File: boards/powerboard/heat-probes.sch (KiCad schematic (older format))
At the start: 16 parts, among them J801 Heat probe power, Q801 BUK7Y4R8-60E, Q802 BUK7Y4R8-60E, Q803 BUK7Y4R8-60E, U801 ACS711, U802 ACS711, U803 ACS711

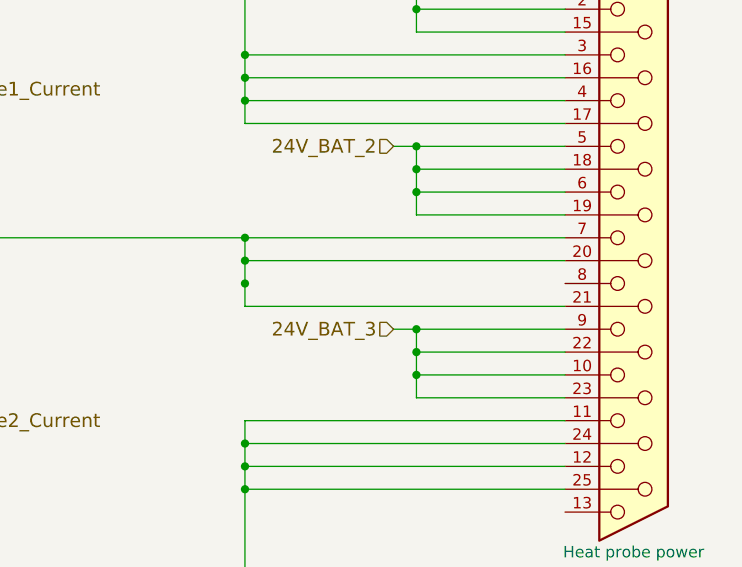
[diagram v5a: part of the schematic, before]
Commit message: [powerboard] layout: parts placed; RS-422 termination added; various minor improvements
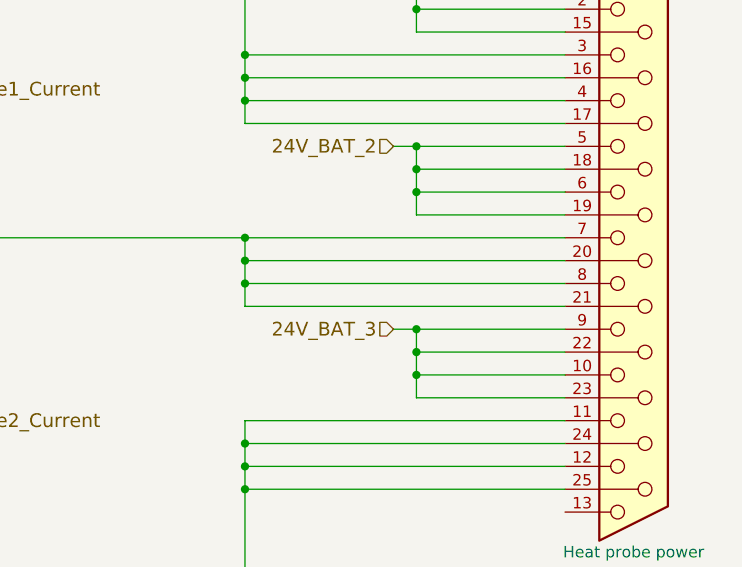
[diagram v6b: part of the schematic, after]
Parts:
- J801: footprint Mounting_Holes:MountingHole_3.2mm_M3_Pad_Via -> Connectors:DB25FD
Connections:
- net at J801.20 (P20), J801.21 (P21), J801.7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: now also J801.8
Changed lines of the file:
@@
 $EndDescr
 $Comp
-L GND #PWR058
+L GND #PWR060
 U 1 1 58F51ACB
 P 6250 5800
-F 0 "#PWR058" H 6250 5550 50  0001 C CNN
+F 0 "#PWR060" H 6250 5550 50  0001 C CNN
 F 1 "GND" H 6250 5650 50  0000 C CNN
 F 2 "" H 6250 5800 50  0000 C CNN
@@
 $EndComp
 $Comp
-L GND #PWR059
+L GND #PWR061
 U 1 1 58F51AEC
 P 5050 5900
-F 0 "#PWR059" H 5050 5650 50  0001 C CNN
+F 0 "#PWR061" H 5050 5650 50  0001 C CNN
 F 1 "GND" H 5050 5750 50  0000 C CNN
 F 2 "" H 5050 5900 50  0000 C CNN
@@
 $EndComp
 $Comp
-L GND #PWR060
+L GND #PWR062
 U 1 1 58F51AF2
 P 5050 3050
-F 0 "#PWR060" H 5050 2800 50  0001 C CNN
+F 0 "#PWR062" H 5050 2800 50  0001 C CNN
 F 1 "GND" H 5050 2900 50  0000 C CNN
 F 2 "" H 5050 3050 50  0000 C CNN
@@
 $EndComp
 $Comp
-L GND #PWR061
+L GND #PWR063
 U 1 1 58F51AF8
 P 5050 4500
-F 0 "#PWR061" H 5050 4250 50  0001 C CNN
+F 0 "#PWR063" H 5050 4250 50  0001 C CNN
 F 1 "GND" H 5050 4350 50  0000 C CNN
 F 2 "" H 5050 4500 50  0000 C CNN
@@
 $EndComp
 $Comp
-L GND #PWR062
+L GND #PWR064
 U 1 1 58F51AFE
 P 6250 4400
-F 0 "#PWR062" H 6250 4150 50  0001 C CNN
+F 0 "#PWR064" H 6250 4150 50  0001 C CNN
 F 1 "GND" H 6250 4250 50  0000 C CNN
 F 2 "" H 6250 4400 50  0000 C CNN
@@
 $EndComp
 $Comp
-L GND #PWR063
+L GND #PWR065
 U 1 1 58F51B04
 P 6250 2950
-F 0 "#PWR063" H 6250 2700 50  0001 C CNN
+F 0 "#PWR065" H 6250 2700 50  0001 C CNN
 F 1 "GND" H 6250 2800 50  0000 C CNN
 F 2 "" H 6250 2950 50  0000 C CNN
@@
 $EndComp
 $Comp
-L +3V3 #PWR064
+L +3V3 #PWR066
 U 1 1 58F51B0A
 P 6250 5500
-F 0 "#PWR064" H 6250 5350 50  0001 C CNN
+F 0 "#PWR066" H 6250 5350 50  0001 C CNN
 F 1 "+3V3" H 6250 5640 50  0000 C CNN
 F 2 "" H 6250 5500 50  0000 C CNN
@@
 $EndComp
 $Comp
-L +3V3 #PWR065
+L +3V3 #PWR067
 U 1 1 58F51B10
 P 6250 4100
-F 0 "#PWR065" H 6250 3950 50  0001 C CNN
+F 0 "#PWR067" H 6250 3950 50  0001 C CNN
 F 1 "+3V3" H 6250 4240 50  0000 C CNN
 F 2 "" H 6250 4100 50  0000 C CNN
@@
 $EndComp
 $Comp
-L +3V3 #PWR066
+L +3V3 #PWR068
 U 1 1 58F51B16
 P 6250 2650
-F 0 "#PWR066" H 6250 2500 50  0001 C CNN
+F 0 "#PWR068" H 6250 2500 50  0001 C CNN
 F 1 "+3V3" H 6250 2790 50  0000 C CNN
 F 2 "" H 6250 2650 50  0000 C CNN
@@
 $EndComp
 $Comp
-L +3V3 #PWR067
+L +3V3 #PWR069
 U 1 1 58F51B37
 P 4750 6600
-F 0 "#PWR067" H 4750 6450 50  0001 C CNN
+F 0 "#PWR069" H 4750 6450 50  0001 C CNN
 F 1 "+3V3" H 4750 6740 50  0000 C CNN
 F 2 "" H 4750 6600 50  0000 C CNN
@@
 $EndComp
 $Comp
-L GND #PWR068
+L GND #PWR070
 U 1 1 58F51B3D
 P 4750 7100
-F 0 "#PWR068" H 4750 6850 50  0001 C CNN
+F 0 "#PWR070" H 4750 6850 50  0001 C CNN
 F 1 "GND" H 4750 6950 50  0000 C CNN
 F 2 "" H 4750 7100 50  0000 C CNN
@@
 F 0 "J801" H 10200 4750 50  0000 C CNN
 F 1 "Heat probe power" H 10200 2025 50  0000 C CNN
-F 2 "Mounting_Holes:MountingHole_3.2mm_M3_Pad_Via" H 10200 3400 50  0001 C CNN
+F 2 "Connectors:DB25FD" H 10200 3400 50  0001 C CNN
 F 3 "" H 10200 3400 50  0001 C CNN
 	1    10200 3400
@@
 Connection ~ 8500 3400
 Connection ~ 3800 3200
+Wire Wire Line
+	9900 3600 8500 3600
 $EndSCHEMATC

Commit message: [powerboard] first layout (wip)
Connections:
- net Probe1: now also J801.16 (P16), J801.17 (P17), J801.3, J801.4, Q801.5 (D); no longer Q801.1 (S), Q801.2 (S), Q801.3 (S), R804.1, U801.1 (IP+), U801.2 (IP+)
- net Probe2: now also J801.20 (P20), J801.21 (P21), J801.7, J801.8, Q802.5 (D); no longer Q802.1 (S), Q802.2 (S), Q802.3 (S), R805.1, U802.1 (IP+), U802.2 (IP+)
- net Probe3: now also J801.11, J801.12, J801.24 (P24), J801.25 (P25), Q803.5 (D); no longer Q803.1 (S), Q803.2 (S), Q803.3 (S), R806.1, U803.1 (IP+), U803.2 (IP+)
- new net Probe1_sense: Q801.1 (S), Q801.2 (S), Q801.3 (S), R804.1, U801.1 (IP+), U801.2 (IP+)
- new net Probe2_sense: Q802.1 (S), Q802.2 (S), Q802.3 (S), R805.1, U802.1 (IP+), U802.2 (IP+)
- new net Probe3_sense: Q803.1 (S), Q803.2 (S), Q803.3 (S), R806.1, U803.1 (IP+), U803.2 (IP+)
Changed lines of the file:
@@
 $EndDescr
 $Comp
-L GND #PWR711
+L GND #PWR060
 U 1 1 58F51ACB
 P 6250 5800
-F 0 "#PWR711" H 6250 5550 50  0001 C CNN
+F 0 "#PWR060" H 6250 5550 50  0001 C CNN
 F 1 "GND" H 6250 5650 50  0000 C CNN
 F 2 "" H 6250 5800 50  0000 C CNN
@@
 	0    -1   -1   0
 $EndComp
-Text Label 4450 2750 0    60   ~ 0
-Probe1
-Text Label 4200 4200 0    60   ~ 0
-Probe2
-Text Label 4550 5600 0    60   ~ 0
-Probe3
+Text Label 3900 2750 0    60   ~ 0
+Probe1_sense
+Text Label 3900 4200 0    60   ~ 0
+Probe2_sense
+Text Label 3900 5600 0    60   ~ 0
+Probe3_sense
 Text Label 2800 3900 2    60   ~ 0
 Probe2_EN
@@
 $EndComp
 $Comp
-L GND #PWR705
+L GND #PWR061
 U 1 1 58F51AEC
 P 5050 5900
-F 0 "#PWR705" H 5050 5650 50  0001 C CNN
+F 0 "#PWR061" H 5050 5650 50  0001 C CNN
 F 1 "GND" H 5050 5750 50  0000 C CNN
 F 2 "" H 5050 5900 50  0000 C CNN
@@
 $EndComp
 $Comp
-L GND #PWR703
+L GND #PWR062
 U 1 1 58F51AF2
 P 5050 3050
-F 0 "#PWR703" H 5050 2800 50  0001 C CNN
+F 0 "#PWR062" H 5050 2800 50  0001 C CNN
 F 1 "GND" H 5050 2900 50  0000 C CNN
 F 2 "" H 5050 3050 50  0000 C CNN
@@
 $EndComp
 $Comp
-L GND #PWR704
+L GND #PWR063
 U 1 1 58F51AF8
 P 5050 4500
-F 0 "#PWR704" H 5050 4250 50  0001 C CNN
+F 0 "#PWR063" H 5050 4250 50  0001 C CNN
 F 1 "GND" H 5050 4350 50  0000 C CNN
 F 2 "" H 5050 4500 50  0000 C CNN
@@
 $EndComp
 $Comp
-L GND #PWR709
+L GND #PWR064
 U 1 1 58F51AFE
 P 6250 4400
-F 0 "#PWR709" H 6250 4150 50  0001 C CNN
+F 0 "#PWR064" H 6250 4150 50  0001 C CNN
 F 1 "GND" H 6250 4250 50  0000 C CNN
 F 2 "" H 6250 4400 50  0000 C CNN
@@
 $EndComp
 $Comp
-L GND #PWR707
+L GND #PWR065
 U 1 1 58F51B04
 P 6250 2950
-F 0 "#PWR707" H 6250 2700 50  0001 C CNN
+F 0 "#PWR065" H 6250 2700 50  0001 C CNN
 F 1 "GND" H 6250 2800 50  0000 C CNN
 F 2 "" H 6250 2950 50  0000 C CNN
@@
 $EndComp
 $Comp
-L +3V3 #PWR710
+L +3V3 #PWR066
 U 1 1 58F51B0A
 P 6250 5500
-F 0 "#PWR710" H 6250 5350 50  0001 C CNN
+F 0 "#PWR066" H 6250 5350 50  0001 C CNN
 F 1 "+3V3" H 6250 5640 50  0000 C CNN
 F 2 "" H 6250 5500 50  0000 C CNN
@@
 $EndComp
 $Comp
-L +3V3 #PWR708
+L +3V3 #PWR067
 U 1 1 58F51B10
 P 6250 4100
-F 0 "#PWR708" H 6250 3950 50  0001 C CNN
+F 0 "#PWR067" H 6250 3950 50  0001 C CNN
 F 1 "+3V3" H 6250 4240 50  0000 C CNN
 F 2 "" H 6250 4100 50  0000 C CNN
@@
 $EndComp
 $Comp
-L +3V3 #PWR706
+L +3V3 #PWR068
 U 1 1 58F51B16
 P 6250 2650
-F 0 "#PWR706" H 6250 2500 50  0001 C CNN
+F 0 "#PWR068" H 6250 2500 50  0001 C CNN
 F 1 "+3V3" H 6250 2790 50  0000 C CNN
 F 2 "" H 6250 2650 50  0000 C CNN
@@
 $EndComp
 $Comp
-L +3V3 #PWR701
+L +3V3 #PWR069
 U 1 1 58F51B37
 P 4750 6600
-F 0 "#PWR701" H 4750 6450 50  0001 C CNN
+F 0 "#PWR069" H 4750 6450 50  0001 C CNN
 F 1 "+3V3" H 4750 6740 50  0000 C CNN
 F 2 "" H 4750 6600 50  0000 C CNN
@@
 $EndComp
 $Comp
-L GND #PWR702
+L GND #PWR070
 U 1 1 58F51B3D
 P 4750 7100
-F 0 "#PWR702" H 4750 6850 50  0001 C CNN
+F 0 "#PWR070" H 4750 6850 50  0001 C CNN
 F 1 "GND" H 4750 6950 50  0000 C CNN
 F 2 "" H 4750 7100 50  0000 C CNN
@@
 Wire Wire Line
 	9900 3600 8500 3600
+Text Label 3900 1750 0    60   ~ 0
+Probe1
+Text Label 3900 3200 0    60   ~ 0
+Probe2
+Text Label 3900 4600 0    60   ~ 0
+Probe3
 $EndSCHEMATC
